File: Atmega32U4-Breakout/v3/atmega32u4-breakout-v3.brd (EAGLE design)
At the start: 39.1 x 21.3 mm, 58 parts, among them IC1 REG1117, U1 ATMEGA32U4

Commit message: Add TOP and BOT markers, shuffle some things around
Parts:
- moved LED 1.51 mm to (12.1, 15.0)
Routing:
- net N$22: track 3.57 -> 2.24 mm
- net VUSB: track 12.0 -> 11.0 mm
- net GND: track 66.8 -> 66.2 mm
- net N$9: track 7.44 -> 6.91 mm
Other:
- board text added: "BOT"
- board text added: "TOP"
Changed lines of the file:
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@@
 <?xml version="1.0" encoding="utf-8"?>
 <!DOCTYPE eagle SYSTEM "eagle.dtd">
-<eagle version="6.5.0">
+<eagle version="6.6.0">
 <drawing>
 <settings>
@@
 <setting verticaltext="up"/>
 </settings>
-<grid distance="0.5" unitdist="mm" unit="mm" style="lines" multiple="1" display="no" altdistance="0.125" altunitdist="mm" altunit="mm"/>
+<grid distance="0.125" unitdist="mm" unit="mm" style="lines" multiple="1" display="no" altdistance="0.125" altunitdist="mm" altunit="mm"/>
 <layers>
 <layer number="1" name="Top" color="4" fill="1" visible="yes" active="yes"/>
@@
 <text x="35.433" y="3.048" size="1.27" layer="49" font="vector" rot="R90">6</text>
 <text x="36.703" y="18.288" size="1.27" layer="49" font="vector" rot="R270">4</text>
-<text x="27.698" y="17.768" size="1.778" layer="49" font="vector" rot="R270">D</text>
-<text x="12.998" y="17.393" size="1.778" layer="49" font="vector" rot="R270">B</text>
+<text x="27.698" y="17.643" size="1.778" layer="49" font="vector" rot="R270">D</text>
+<text x="12.248" y="17.768" size="1.778" layer="49" font="vector" rot="R270">B</text>
 <text x="8.712" y="17.263" size="0.8128" layer="49" font="vector">E6</text>
 <text x="11.053" y="18.288" size="1.27" layer="49" font="vector" rot="R270">0</text>
@@
 <rectangle x1="34.875" y1="9.25" x2="35.175" y2="9.55" layer="1"/>
 <rectangle x1="34.375" y1="9.25" x2="34.675" y2="9.55" layer="1"/>
-<wire x1="9.625" y1="16.375" x2="9.25" y2="16.75" width="0.15" layer="49"/>
-<wire x1="9.625" y1="16.375" x2="9.25" y2="16" width="0.15" layer="49"/>
-<wire x1="9.625" y1="16.375" x2="8.875" y2="16.375" width="0.15" layer="49"/>
-<wire x1="8.875" y1="16.375" x2="8.875" y2="17" width="0.15" layer="49"/>
+<wire x1="10.625" y1="15.875" x2="10.375" y2="16.375" width="0.15" layer="49"/>
+<wire x1="10.625" y1="15.875" x2="10" y2="15.875" width="0.15" layer="49"/>
+<wire x1="10.625" y1="15.875" x2="9.375" y2="16.625" width="0.15" layer="49"/>
+<wire x1="9.375" y1="16.625" x2="9.375" y2="17" width="0.15" layer="49"/>
 <text x="22.733" y="3.048" size="1.27" layer="49" font="vector" rot="R90">6</text>
 <text x="20.193" y="3.048" size="1.27" layer="49" font="vector" rot="R90">7</text>
@@
 <vertex x="3.75" y="12.75"/>
 </polygon>
+<text x="32.5" y="14" size="1.27" layer="1" font="vector" ratio="15">TOP</text>
+<text x="28.5" y="10.5" size="1.27" layer="16" font="vector" ratio="15" rot="MR180">BOT</text>
 </plain>
 <attributes>
@@
 <element name="R6" library="rcl" package="R0603" value="150" x="11.742" y="5.008" rot="R180"/>
 <element name="SJ1" library="jumper" package="SJ" value="" x="9.220459375" y="14.18250625" rot="MR90"/>
-<element name="LED" library="led" package="CHIPLED_0805" value="RED" x="11.512" y="16.352" rot="R270"/>
+<element name="LED" library="led" package="CHIPLED_0805" value="RED" x="12.137" y="14.977" rot="R270"/>
 <element name="POWER" library="led" package="CHIPLED_0805" value="GREEN" x="11.75" y="6.625" rot="R270"/>
 <element name="R4" library="rcl" package="R0603" value="10k" x="34.5" y="8" rot="MR0"/>
@@
 </polygon>
 <via x="12.75" y="15.625" extent="1-16" drill="0.4" shape="octagon"/>
-<wire x1="15.25" y1="16" x2="14.898" y2="16.352" width="0.4064" layer="1"/>
-<wire x1="14.898" y1="16.352" x2="12.562" y2="16.352" width="0.4064" layer="1"/>
-<wire x1="12.562" y1="16.352" x2="12.875" y2="16.039" width="0.4064" layer="1"/>
 <via x="9.375" y="8" extent="1-16" drill="0.4" shape="octagon"/>
 <via x="8.625" y="8" extent="1-16" drill="0.4" shape="octagon"/>
@@
 <wire x1="37.75" y1="15" x2="37.875" y2="15.125" width="0.4064" layer="1"/>
 <wire x1="37.75" y1="15" x2="38.125" y2="15" width="0.4064" layer="1"/>
-<wire x1="38.125" y1="15" x2="38.125" y2="8.5" width="0.4064" layer="1"/>
-<wire x1="38.125" y1="8.5" x2="38.125" y2="6.875" width="0.4064" layer="1"/>
+<wire x1="38.125" y1="15" x2="38.125" y2="6.875" width="0.4064" layer="1"/>
 <wire x1="38.125" y1="6.875" x2="37.75" y2="6.875" width="0.4064" layer="1"/>
 <via x="28.625" y="16.625" extent="1-16" drill="0.4" shape="octagon"/>
-<wire x1="14.5" y1="8" x2="10.988" y2="8" width="0.8128" layer="1"/>
+<wire x1="14.5" y1="8" x2="8.625" y2="8" width="0.8128" layer="1"/>
 <wire x1="10.466959375" y1="9.81695625" x2="9.55904375" y2="10.724871875" width="0.4064" layer="16"/>
 <wire x1="9.55904375" y1="10.724871875" x2="9.55904375" y2="11.369040625" width="0.4064" layer="16"/>
@@
 <wire x1="13.116959375" y1="15.31695625" x2="13.777671875" y2="15.31695625" width="0.4064" layer="16"/>
 <wire x1="13.777671875" y1="15.31695625" x2="14.791096875" y2="14.30353125" width="0.4064" layer="16"/>
-<wire x1="12.75" y1="15.625" x2="12.75" y2="16.164" width="0.4064" layer="1"/>
-<wire x1="12.75" y1="16.164" x2="12.562" y2="16.352" width="0.4064" layer="1"/>
-<wire x1="10.988" y1="8" x2="8.625" y2="8" width="0.8128" layer="1"/>
 <wire x1="8.625" y1="8" x2="8.5" y2="8" width="0.8128" layer="1"/>
-<wire x1="8.625" y1="8" x2="8.5" y2="8" width="0.4064" layer="1"/>
 <wire x1="8.5" y1="8" x2="8.332" y2="8.168" width="0.4064" layer="1"/>
 <wire x1="8.332" y1="8.168" x2="7.958" y2="8.168" width="0.4064" layer="1"/>
 <wire x1="12.8" y1="6.625" x2="13.875" y2="6.625" width="0.4064" layer="1"/>
-<wire x1="13.875" y1="6.625" x2="14" y2="6.5" width="0.4064" layer="1"/>
-<wire x1="14" y1="6.5" x2="14.377" y2="6.123" width="0.4064" layer="1"/>
+<wire x1="13.875" y1="6.625" x2="14.377" y2="6.123" width="0.4064" layer="1"/>
 <wire x1="14.377" y1="6.123" x2="14.838" y2="6.123" width="0.4064" layer="1"/>
 <wire x1="13.875" y1="6.625" x2="14.5" y2="7.25" width="0.4064" layer="1"/>
@@
 <wire x1="32.25" y1="16.25" x2="32" y2="16.5" width="0.4064" layer="16"/>
 <wire x1="32" y1="16.5" x2="32" y2="16.75" width="0.4064" layer="16"/>
+<wire x1="15.25" y1="16" x2="14.21" y2="16" width="0.6096" layer="1"/>
+<wire x1="12.75" y1="15.625" x2="13.187" y2="15.188" width="0.4064" layer="1"/>
+<wire x1="13.187" y1="15.188" x2="13.187" y2="14.977" width="0.4064" layer="1"/>
+<wire x1="14.21" y1="16" x2="13.52695625" y2="15.31695625" width="0.6096" layer="1"/>
+<wire x1="13.52695625" y1="15.31695625" x2="13.116959375" y2="15.31695625" width="0.6096" layer="1"/>
+<wire x1="13.116959375" y1="15.31695625" x2="13.187" y2="15.246915625" width="0.6096" layer="1"/>
+<wire x1="13.187" y1="15.246915625" x2="13.187" y2="14.977" width="0.6096" layer="1"/>
 </signal>
 <signal name="AREF">
@@
 <contactref element="U1" pad="4"/>
 <contactref element="R1" pad="2"/>
-<wire x1="15.25" y1="10.75" x2="16.125" y2="11.625" width="0.4064" layer="1"/>
-<wire x1="16.125" y1="11.625" x2="16.125" y2="12.5" width="0.4064" layer="1"/>
-<via x="16.125" y="12.5" extent="1-16" drill="0.4"/>
-<wire x1="16.125" y1="12.5" x2="15.625" y2="13" width="0.4064" layer="16"/>
-<wire x1="15.625" y1="13" x2="14.963259375" y2="13" width="0.4064" layer="16"/>
+<wire x1="15.75" y1="11.25" x2="15.75" y2="12.5" width="0.4064" layer="1"/>
+<via x="15.75" y="12.5" extent="1-16" drill="0.4"/>
+<wire x1="15.75" y1="12.5" x2="15.25" y2="13" width="0.4064" layer="16"/>
+<wire x1="15.25" y1="13" x2="14.963259375" y2="13" width="0.4064" layer="16"/>
 <wire x1="14.963259375" y1="13" x2="14.2254125" y2="13.737846875" width="0.4064" layer="16"/>
 <wire x1="12.85" y1="9.5" x2="14" y2="9.5" width="0.4064" layer="1"/>
-<wire x1="14" y1="9.5" x2="15.25" y2="10.75" width="0.4064" layer="1"/>
+<wire x1="14" y1="9.5" x2="15.75" y2="11.25" width="0.4064" layer="1"/>
 </signal>
 <signal name="N$10">
@@
 <contactref element="IC1" pad="3"/>
 <contactref element="SJ3" pad="2"/>
-<via x="12.25" y="14.125" extent="1-16" drill="0.4"/>
-<wire x1="12.25" y1="14.125" x2="12.25" y2="13.450515625" width="0.4064" layer="16"/>
+<via x="12.25" y="13.625" extent="1-16" drill="0.4"/>
+<wire x1="12.25" y1="13.625" x2="12.25" y2="13.450515625" width="0.4064" layer="16"/>
 <wire x1="12.25" y1="13.450515625" x2="13.094040625" y2="12.606475" width="0.4064" layer="16"/>
 <wire x1="15.25" y1="14" x2="17.1886" y2="14" width="0.8128" layer="1"/>
@@
 <wire x1="15.25" y1="14" x2="14.375" y2="13.125" width="0.8128" layer="1"/>
 <wire x1="14.375" y1="13.125" x2="13.4" y2="13.125" width="0.8128" layer="1"/>
-<wire x1="12.25" y1="14.125" x2="12.25" y2="13.375" width="0.4064" layer="1"/>
-<wire x1="12.25" y1="13.375" x2="12.375" y2="13.25" width="0.4064" layer="1"/>
-<wire x1="12.375" y1="13.25" x2="12.5" y2="13.125" width="0.4064" layer="1"/>
+<wire x1="12.25" y1="13.625" x2="12.25" y2="13.375" width="0.4064" layer="1"/>
+<wire x1="12.25" y1="13.375" x2="12.5" y2="13.125" width="0.4064" layer="1"/>
 <wire x1="12.5" y1="13.125" x2="13.4" y2="13.125" width="0.4064" layer="1"/>
 </signal>
@@
 <contactref element="R5" pad="2"/>
 <contactref element="LED" pad="A"/>
-<via x="11.25" y="15.125" extent="1-16" drill="0.4"/>
-<wire x1="11.25" y1="15.125" x2="10.462" y2="15.913" width="0.4064" layer="1"/>
-<wire x1="10.462" y1="15.913" x2="10.462" y2="16.352" width="0.4064" layer="1"/>
+<via x="11.25" y="16.125" extent="1-16" drill="0.4"/>
 <wire x1="11.6" y1="17" x2="11.25" y2="16.65" width="0.4064" layer="16"/>
-<wire x1="11.25" y1="16.65" x2="11.25" y2="15.125" width="0.4064" layer="16"/>
+<wire x1="11.25" y1="16.65" x2="11.25" y2="16.125" width="0.4064" layer="16"/>
+<wire x1="11.087" y1="14.977" x2="11.25" y2="15.14" width="0.4064" layer="1"/>
+<wire x1="11.25" y1="15.14" x2="11.25" y2="16.125" width="0.4064" layer="1"/>
 </signal>
 <signal name="N$4">

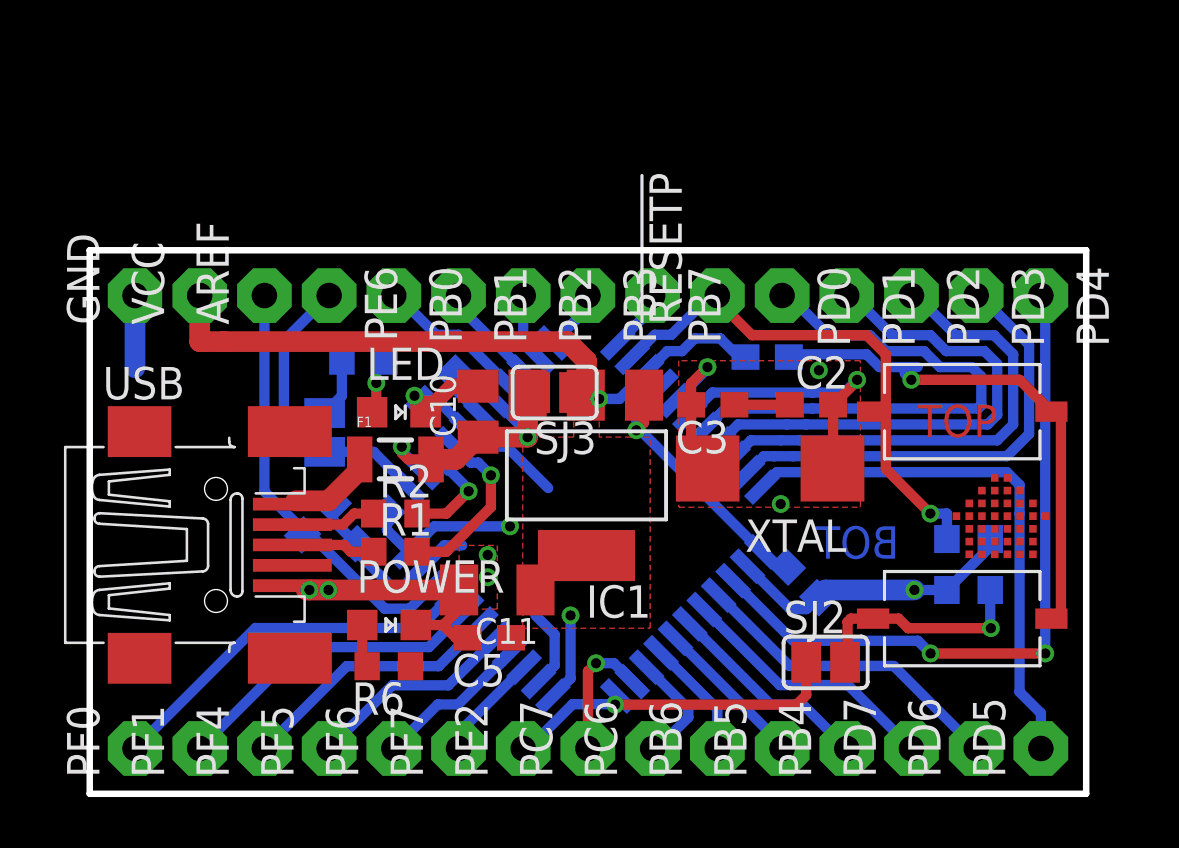
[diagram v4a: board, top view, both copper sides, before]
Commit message: Nudge some more stuff around, change silkscreen, add large GND pad on bottom, add multicb gerber job
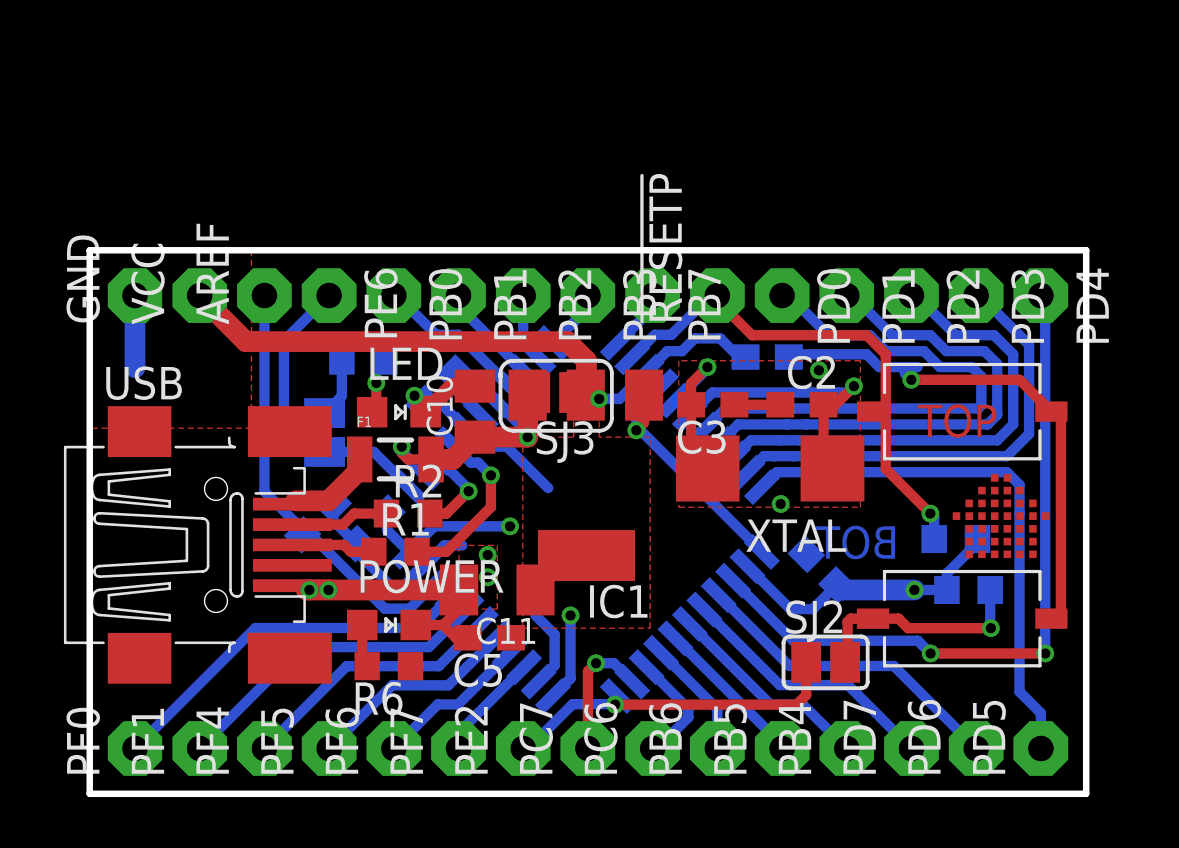
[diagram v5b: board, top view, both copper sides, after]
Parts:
- IC1: value REG1117 -> REG1117NP; device burr-brown:SOT223 -> burr-brown:SOT223-NP
- SJ3: device jumper:SJ -> jumper:SJNP
- moved C8 0.90 mm to (28.7, 8.80)
- moved R2 0.50 mm to (12.5, 11.0)
- moved R3 0.50 mm to (34.0, 10.0)
- moved C2 0.38 mm to (28.0, 15.3)
- moved C10 0.12 mm to (15.1, 15.0)
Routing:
- net VCC: track 47.5 -> 46.4 mm
- net !RESET: track 21.5 -> 20.9 mm
- net N$2: track 3.37 -> 3.87 mm
- net N$10: track 4.19 -> 3.69 mm
- net GND: track 66.2 -> 65.7 mm
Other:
- board text added: "E2= BOOT"
- board text added: "E6=LED"
- board text added: "VDD =VUSB"

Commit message: Change red LED to blue, adapt dropper resistor
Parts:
- LED: value RED -> BLUE
- R6: value 150 -> 820
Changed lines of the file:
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@@
 <layers>
 <layer number="1" name="Top" color="4" fill="1" visible="yes" active="yes"/>
-<layer number="16" name="Bottom" color="1" fill="1" visible="yes" active="yes"/>
+<layer number="16" name="Bottom" color="1" fill="1" visible="no" active="yes"/>
 <layer number="17" name="Pads" color="2" fill="1" visible="yes" active="yes"/>
 <layer number="18" name="Vias" color="2" fill="1" visible="yes" active="yes"/>
@@
 <layer number="20" name="Dimension" color="15" fill="1" visible="yes" active="yes"/>
 <layer number="21" name="tPlace" color="7" fill="1" visible="yes" active="yes"/>
-<layer number="22" name="bPlace" color="7" fill="1" visible="yes" active="yes"/>
+<layer number="22" name="bPlace" color="7" fill="1" visible="no" active="yes"/>
 <layer number="23" name="tOrigins" color="15" fill="1" visible="yes" active="yes"/>
-<layer number="24" name="bOrigins" color="15" fill="1" visible="yes" active="yes"/>
-<layer number="25" name="tNames" color="7" fill="1" visible="no" active="yes"/>
+<layer number="24" name="bOrigins" color="15" fill="1" visible="no" active="yes"/>
+<layer number="25" name="tNames" color="7" fill="1" visible="yes" active="yes"/>
 <layer number="26" name="bNames" color="7" fill="1" visible="no" active="yes"/>
-<layer number="27" name="tValues" color="7" fill="1" visible="no" active="yes"/>
+<layer number="27" name="tValues" color="7" fill="1" visible="yes" active="yes"/>
 <layer number="28" name="bValues" color="7" fill="1" visible="no" active="yes"/>
 <layer number="29" name="tStop" color="7" fill="3" visible="no" active="yes"/>
@@
 <layer number="37" name="tTest" color="7" fill="1" visible="no" active="yes"/>
 <layer number="38" name="bTest" color="7" fill="1" visible="no" active="yes"/>
-<layer number="39" name="tKeepout" color="4" fill="11" visible="no" active="yes"/>
+<layer number="39" name="tKeepout" color="4" fill="11" visible="yes" active="yes"/>
 <layer number="40" name="bKeepout" color="1" fill="11" visible="no" active="yes"/>
 <layer number="41" name="tRestrict" color="4" fill="10" visible="yes" active="yes"/>
-<layer number="42" name="bRestrict" color="1" fill="10" visible="yes" active="yes"/>
+<layer number="42" name="bRestrict" color="1" fill="10" visible="no" active="yes"/>
 <layer number="43" name="vRestrict" color="2" fill="10" visible="yes" active="yes"/>
 <layer number="44" name="Drills" color="7" fill="1" visible="no" active="yes"/>
@@
 <layer number="50" name="dxf" color="7" fill="1" visible="yes" active="yes"/>
 <layer number="51" name="tDocu" color="7" fill="1" visible="yes" active="yes"/>
-<layer number="52" name="bDocu" color="7" fill="1" visible="yes" active="yes"/>
+<layer number="52" name="bDocu" color="7" fill="1" visible="no" active="yes"/>
 <layer number="53" name="tGND_GNDA" color="7" fill="9" visible="no" active="no"/>
 <layer number="54" name="bGND_GNDA" color="1" fill="9" visible="no" active="no"/>
@@
 <layer number="104" name="Name" color="7" fill="1" visible="yes" active="yes"/>
 <layer number="105" name="Beschreib" color="9" fill="1" visible="yes" active="yes"/>
-<layer number="106" name="BGA-Top" color="4" fill="1" visible="yes" active="yes"/>
+<layer number="106" name="BGA-Top" color="4" fill="1" visible="no" active="yes"/>
 <layer number="107" name="BD-Top" color="5" fill="1" visible="yes" active="yes"/>
 <layer number="108" name="fp8" color="7" fill="1" visible="no" active="yes"/>
@@
 <element name="VCC" library="jocki" package="2,15/1,0-NOPLACE" value="WIREPAD2,15/1,0-NOPLACE" x="4.318" y="19.558" rot="R90"/>
 <element name="R5" library="rcl" package="R0603" value="180" x="10.75" y="17" rot="MR180"/>
-<element name="R6" library="rcl" package="R0603" value="150" x="11.742" y="5.008" rot="R180"/>
+<element name="R6" library="rcl" package="R0603" value="820" x="11.742" y="5.008" rot="R180"/>
 <element name="SJ1" library="jumper" package="SJ" value="" x="9.220459375" y="14.18250625" rot="MR90"/>
-<element name="LED" library="led" package="CHIPLED_0805" value="RED" x="12.137" y="14.977" rot="R270"/>
+<element name="LED" library="led" package="CHIPLED_0805" value="BLUE" x="12.137" y="14.977" rot="R270"/>
 <element name="POWER" library="led" package="CHIPLED_0805" value="GREEN" x="11.75" y="6.625" rot="R270"/>
 <element name="R4" library="rcl" package="R0603" value="10k" x="34.5" y="8" rot="MR0"/>
